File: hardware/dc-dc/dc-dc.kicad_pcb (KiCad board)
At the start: 4 copper layers, 49.9 x 49.9 mm, 28 parts, among them J1 Conn_01x06, J2 Screw_Terminal_01x02, J3 Screw_Terminal_01x02, U1 MP8859GQ-0000-P

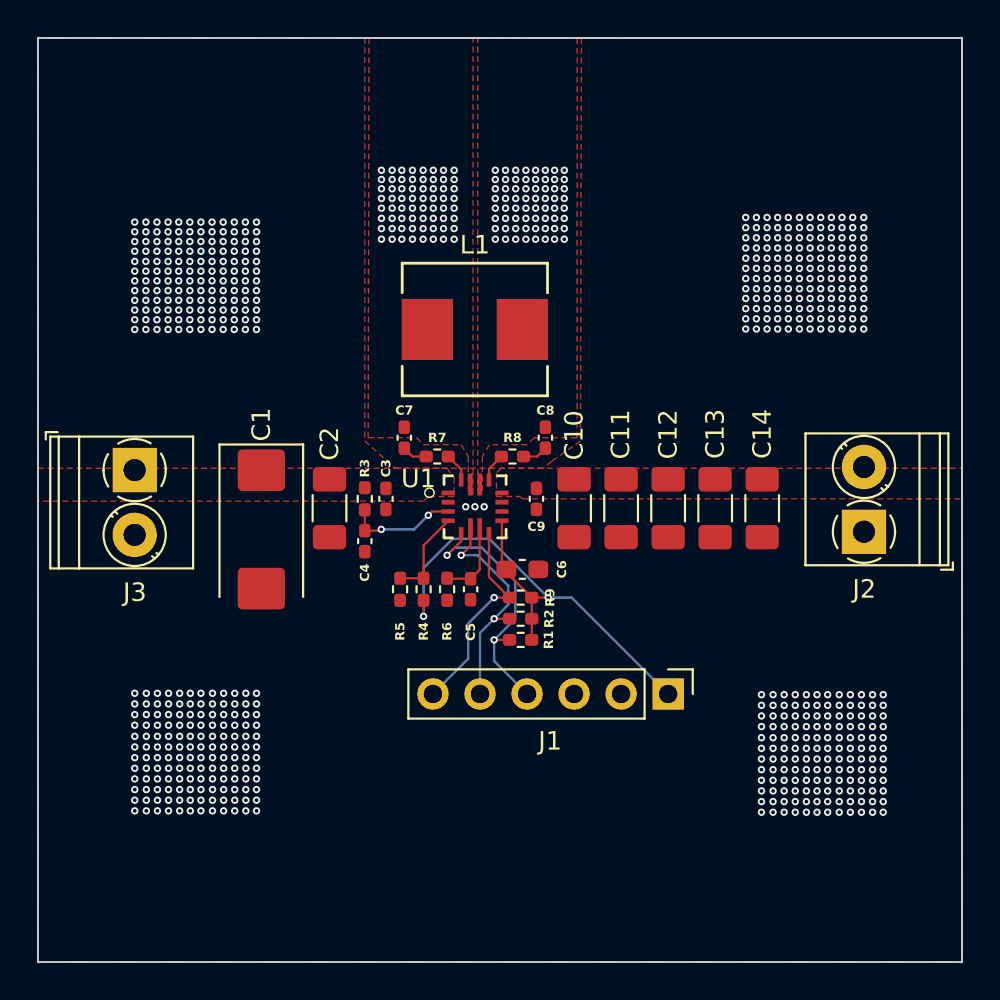
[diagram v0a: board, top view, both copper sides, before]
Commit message: [Schematic/PCB] Add qwiic connector and 2 electrolytic caps
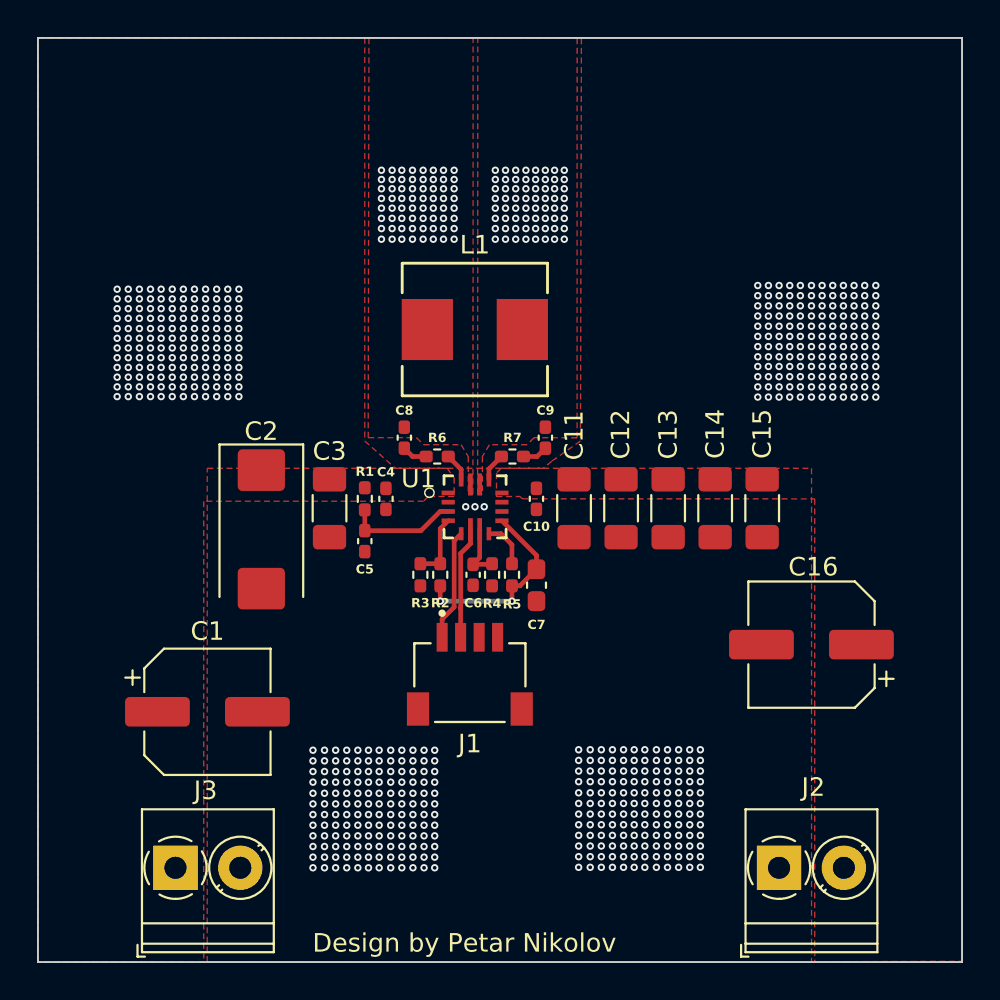
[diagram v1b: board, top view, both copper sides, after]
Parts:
- removed the R1 at (154.5, 82.0)
- removed the R2 at (154.5, 80.9)
- added C1: 100u, Capacitor_SMD:CP_Elec_6.3x7.7, F.Cu at (137.6, 85.9)
- added C16: 100u, Capacitor_SMD:CP_Elec_6.3x7.7, F.Cu at (170.2, 82.3)
- J1: value Conn_01x06 -> PRT-14417; footprint Connector_PinHeader_2.54mm:PinHeader_1x06_P2.54mm_Vertical -> QWIIC:SPARKFUN_PRT-14417
- moved J3 21.6 mm to (135.8, 94.3), turned to 0 degrees
- moved J2 18.7 mm to (168.4, 94.3), turned to 0 degrees
- moved J1 10.7 mm to (151.7, 84.3), turned to 0 degrees
- moved R4 2.55 mm to (152.9, 78.5)
- moved R3 1.35 mm to (149.1, 78.5)
- moved R5 1.32 mm to (154.0, 78.5), turned to -90 degrees
- moved R2 1.19 mm to (150.1, 78.5)
- moved C7 1.15 mm to (155.3, 79.1), turned to -90 degrees
- moved C6 0.79 mm to (151.9, 78.5)
- renumbered C9 to C10, C10 to C11, C11 to C12, C12 to C13, C13 to C14, C14 to C15, C1 to C2, C2 to C3, C3 to C4, C4 to C5, C5 to C6, C6 to C7, C7 to C8, C8 to C9, R3 to R1, R4 to R2, R5 to R3, R6 to R4, R9 to R5, R7 to R6, R8 to R7
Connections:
- J1 pad 1: VCC -> /SCL
- J1 pad 2: GND -> /SDA
- J1 pad 3: GND -> unconnected-(J1-Pad3)
- J1 pad 4: /SCL -> GND
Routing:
- net VCC: track 28.8 -> 10.6 mm
- net /ALT: track 11.3 -> 2.52 mm, vias 1 -> 0
- net /SCL: track 14.2 -> 6.02 mm, vias 2 -> 0
- net /SDA: track 12.1 -> 6.05 mm, vias 2 -> 0
- net Net-(U1-ADD): track 4.93 -> 3.57 mm
- net Net-(U1-OC): track 4.16 -> 3.08 mm
- net Net-(U1-EN): vias 2 -> 0
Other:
- board text added: "Design by Petar Nikolov"
